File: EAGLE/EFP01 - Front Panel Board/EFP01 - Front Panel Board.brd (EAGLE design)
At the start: 200 x 65 mm, 150 parts, among them J1 PWRBTN, J16 S8B-PH-SM4, J17 S8B-PH-SM4, J18 S6B-PH-SM4, J2 ESTOP, J20 Intel EDISON, J3 USB-A(2.0), J5 LCD, J6 S8B-PH-SM4, J7 USB-B, Q2 25MHz, U1 74LVC1T45, U10 FT231XS-R, U11 74LVC1T45, U12 74LVC1T45, U13 74LVC1T45, U14 74LVC1T45, U15 74LVC1T45, U17 OR, U18 MIC2026-1YM, U19 MIC2026-1YM, U2 74LVC1T45, U20 OR, U21 74LVC1T45, U22 74LVC1T45, U23 74LVC1T45, U24 74LVC1T45, U25 74LVC1T45, U26 74LVC1T45, U27 74LVC1T45, U28 74LVC1T45, U3 93LC66A, U30 74LVC1T45, U4 LAN9514, U5 74LVC1T45, U6 74LVC1T45, U7 74LVC1T45, U8 74LVC1T45, U9 SP3485

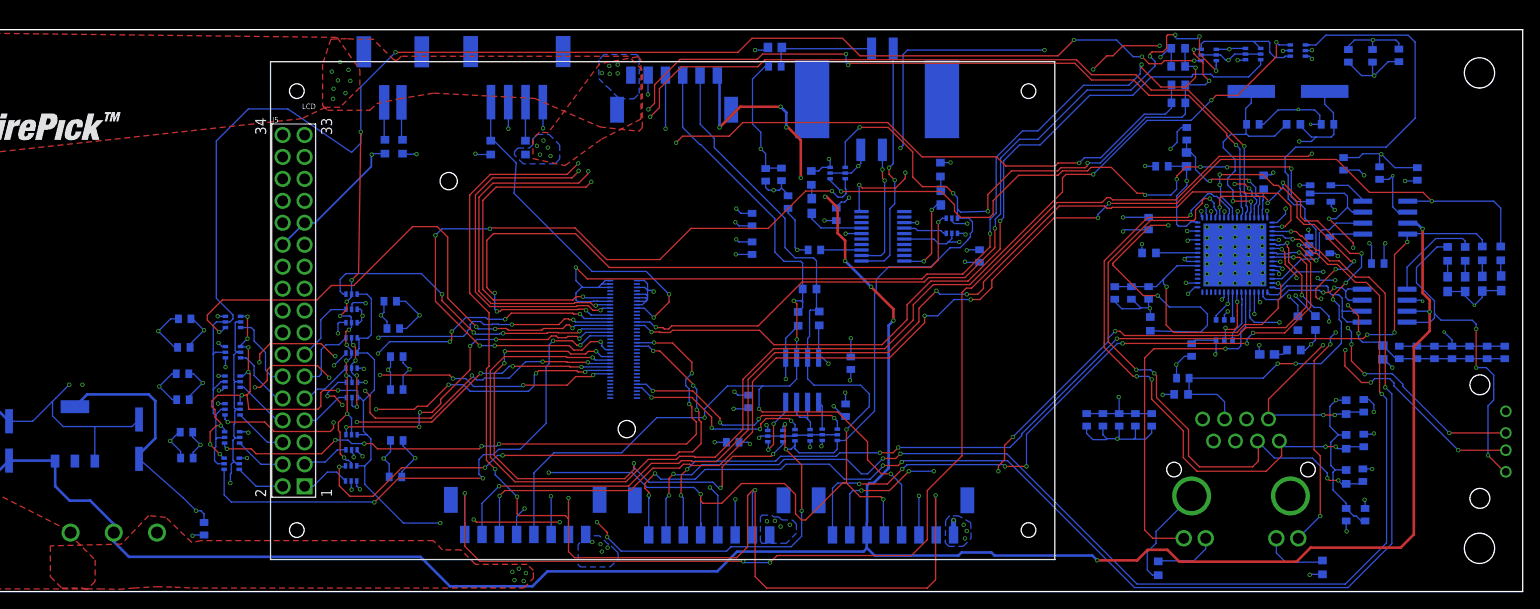
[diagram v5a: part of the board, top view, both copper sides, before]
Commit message: Partially-routed diff pairs
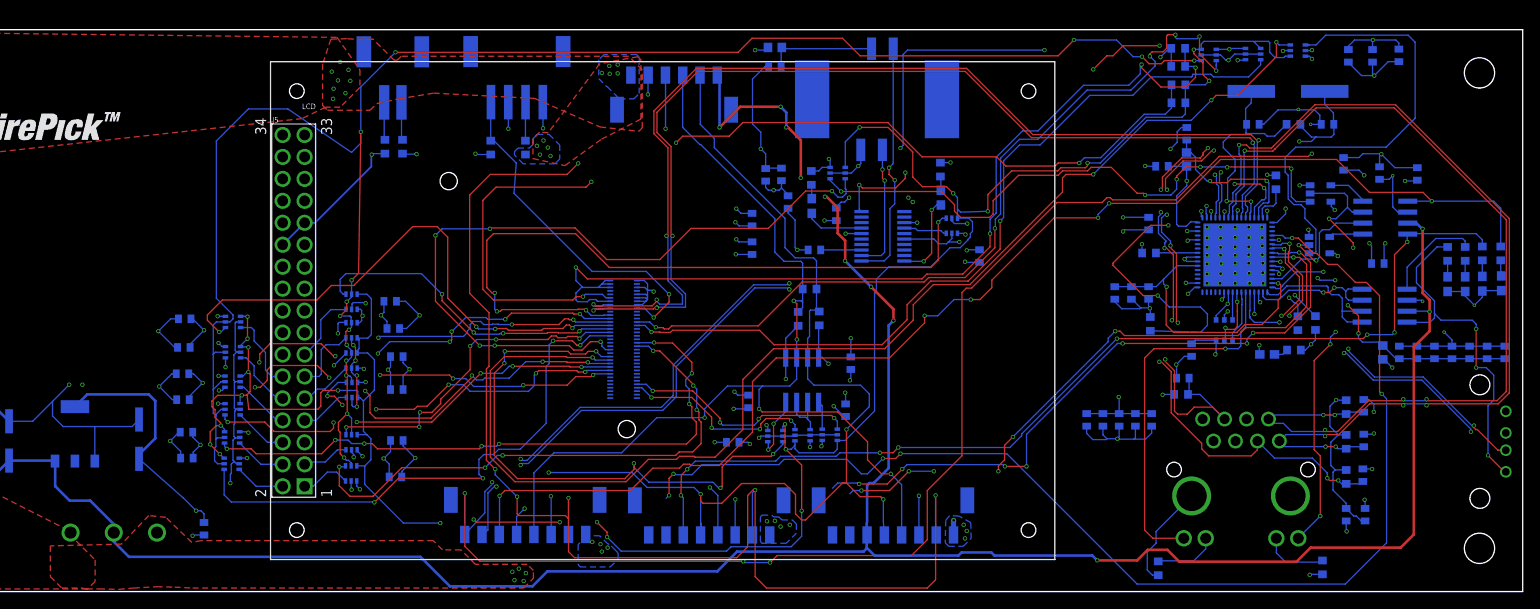
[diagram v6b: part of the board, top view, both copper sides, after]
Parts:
- moved R35 1.42 mm to (171.4, 47.3)
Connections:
- net EE_D+ renamed EE_P
- net EE_D- renamed EE_N
- net RD+ renamed RD_P
- net RD- renamed RD_N
- net TD+ renamed TD_P
- net TD- renamed TD_N
- net ULC_D+ renamed ULC_P
- net ULC_D- renamed ULC_N
- net USBA_D+ renamed USBA_P
- net USBA_D- renamed USBA_N
- net USBDM0 renamed USB0_N
- net USBDP0 renamed USB0_P
- net USBMCU+ renamed USBMCU_P
- net USBMCU- renamed USBMCU_N
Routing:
- net EE_N: track 149.3 -> 0.00 mm, vias 6 -> 0
- net ULC_N: track 154.9 -> 235.9 mm, vias 5 -> 9
- net TD_N: track 61.8 -> 108.3 mm, vias 8 -> 6
- net ULC_P: track 122.3 -> 81.1 mm
- net TD_P: track 72.1 -> 108.4 mm, vias 5 -> 6
- net USB0_N: track 141.3 -> 122.2 mm, vias 6 -> 4
- net USB0_P: track 139.3 -> 122.8 mm
- net USBMCU_N: track 82.4 -> 77.0 mm
- net RD_N: track 65.1 -> 60.3 mm, vias 8 -> 7
- net USBMCU_P: track 77.8 -> 73.0 mm
- net EE_P: track 144.8 -> 140.6 mm
- net USBA_P: track 39.3 -> 43.5 mm, vias 6 -> 4
- net RD_P: track 71.3 -> 75.4 mm, vias 5 -> 9
- net VDD18USB: track 16.0 -> 18.4 mm
- net XI: track 27.5 -> 29.6 mm
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
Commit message: Final(??) Versions of FPD boards.
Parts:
- moved U12 43.4 mm to (133.7, 36.7), turned to 0 degrees
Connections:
- net DM renamed SCON_N
- net DP renamed SCON_P
- net RXD renamed SC_N
- net RXDO renamed SCED_N
- net TXD renamed SCED_P
- net TXDO renamed SC_P
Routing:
- net EE_N: track 0.00 -> 121.0 mm, vias 0 -> 8
- net ULC_P: track 81.1 -> 167.0 mm, vias 4 -> 9
- net ULC_N: track 235.9 -> 171.6 mm
- net SC_P: track 69.4 -> 13.5 mm, vias 7 -> 3
- net SCED_P: track 94.4 -> 53.9 mm, vias 2 -> 6
- net N$9: track 0.00 -> 37.8 mm
- net N$4: track 0.00 -> 37.8 mm
- net EE_P: track 140.6 -> 120.4 mm, vias 6 -> 9
- net EXRES: track 37.9 -> 23.9 mm, vias 3 -> 4
- net SCED_N: track 82.4 -> 72.5 mm, vias 4 -> 9
- net +1V8: track 272.5 -> 281.7 mm
- net 74DIR: track 94.1 -> 101.1 mm, vias 6 -> 8
- net N$21: track 109.5 -> 113.5 mm, vias 4 -> 6
- net GND: track 349.2 -> 345.7 mm, vias 107 -> 109
- net RD_N: track 60.3 -> 58.5 mm, vias 7 -> 3
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
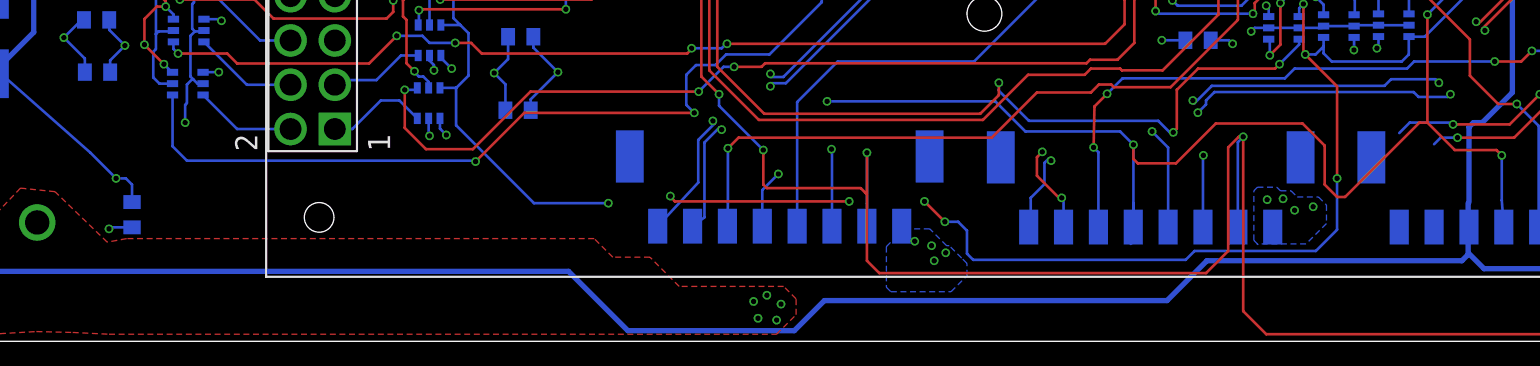
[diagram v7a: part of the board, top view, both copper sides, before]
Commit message: Created BOM for EFP01
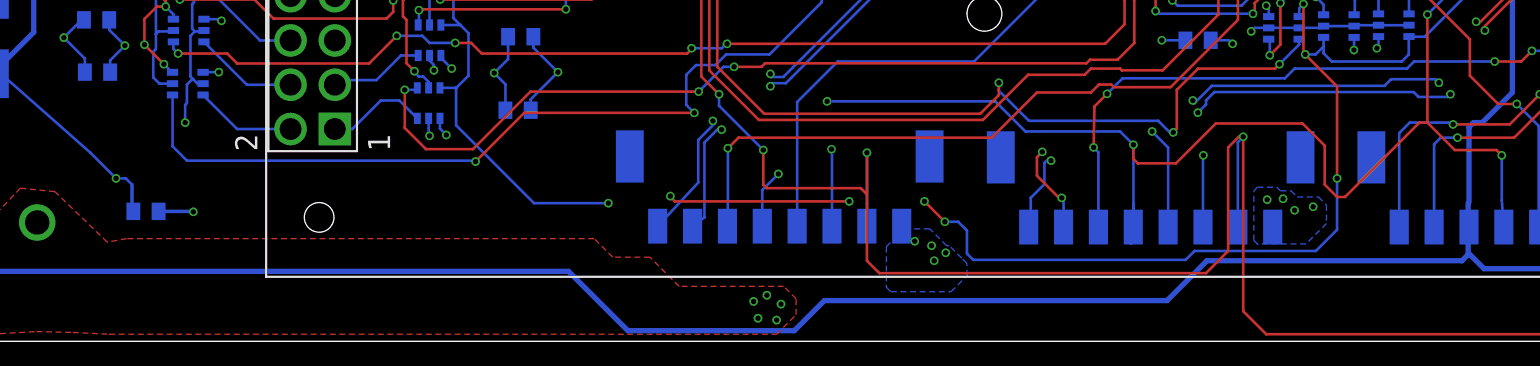
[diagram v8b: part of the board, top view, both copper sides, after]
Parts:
- moved C2 0.82 mm to (48.2, 7.45), turned to 0 degrees
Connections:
- net +3V3: now also C2.2; no longer C2.1
- net GND: now also C2.1; no longer C2.2
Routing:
- net USBMCU_N: track 77.0 -> 82.4 mm
- net USBMCU_P: track 73.0 -> 77.8 mm
- net GND: track 345.7 -> 346.4 mm
- net +3V3: track 214.0 -> 214.6 mm
